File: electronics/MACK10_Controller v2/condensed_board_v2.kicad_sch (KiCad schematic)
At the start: 81 parts, among them J13 LOAD_CELL, J14 CHANNEL_B, J15 Motor, J16 AS5600 Encoder, J17 Fan, J18 Conn_01x02, J19 24V IN, J20 I/O, J21 LIM_TOP, J22 LIM_BOT, J23 INPUT, J24 E_STOP, J25 SSD1306, J26 Load Cell, J27 USER_STATUS_LED, J28 LOAD_CELL, Q3 MMBT3906, Q4 MMBT3906, U5 TMC2208, U8 HX711, U9 HX711

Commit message: Various PCB Schematic Updates
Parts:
- removed C10, C11, C12, C17, C18: 0.1uF, symbol Device:C
- removed C13, C15: 10uF, symbol Device:C
- removed J13: LOAD_CELL, symbol Connector_Generic:Conn_01x05
- removed J14: CHANNEL_B, symbol Connector_Generic:Conn_01x02
- removed J26: Load Cell, Connector_JST:JST_XH_B4B-XH-A_1x04_P2.50mm_Vertical, symbol MACK10:LOAD_CELL_4P
- removed JP3: Solder Jumper, symbol Jumper:SolderJumper_2_Bridged
- removed L2: 3.3uH, symbol Device:L
- removed Q3: MMBT3906, Package_TO_SOT_SMD:SOT-23, symbol Transistor_BJT:MMBT3906
- removed R10: 20k, symbol Device:R_US
- removed R11: 8.2k, symbol Device:R_US
- removed R12, R13: 100, symbol Device:R_US
- removed R14: 10k, symbol Device:R_US
- removed TP22: HX_SCK, TestPoint:TestPoint_Pad_2.0x2.0mm, symbol Connector:TestPoint
- removed TP23: HX_DT, TestPoint:TestPoint_Pad_2.0x2.0mm, symbol Connector:TestPoint
- removed U8: HX711, Package_SO:SOIC-16_3.9x9.9mm_P1.27mm, symbol Analog_ADC:HX711
- U9: symbol Analog_ADC:HX711 -> MACK10:HX711_IC
- renumbered J_EXPANSION to J_EXPANSION1
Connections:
- net 5V is gone; now on net +5V: J_EXPANSION1.3 (Pin_3)
- net +24V: now also U14.1 (VIN+); no longer U14. (VOUT-)
- net +5V: now also U14.3 (VOUT+); no longer U14. (VOUT-)
- net 3V3: now also U13.8 (VCC); no longer U13. (IN-)
- net GND: now also U13.7 (GND), U14.2 (VIN-), U14.4 (VOUT-); no longer C14.2, C16.2, U13. (IN-), U14. (VOUT-)
- net MOTOR_24V: now also U13.1 (IN+); no longer U13. (IN-)
- net MOTOR_VMOT: now also U13.2 (IN-), U13.3 (VBUS); no longer U13. (IN-)
- net SCL: now also U13.5 (SCL); no longer U13. (IN-)
- net SDA: now also U13.6 (SDA); no longer U13. (IN-)
- net UP: now also U12.8 (P00)
- net IO0: no longer names the net of J_EXPANSION1.6 (Pin_6)
- net IO0: no longer U12.8 (P00)
- new net: C14.2, C16.2
- no-connect marks 11 -> 22
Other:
- note removed: "AVDD = VBG(R1+R2)/R1"
- note removed: "Jumper Default: Closed Data rate set to 10SPS Open jumper to set to 80SPS Increases noise per read"
- moved on the sheet: C14, C16, C19, C21, C22, Q4, TP14, U5

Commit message: Minor PCB Changes
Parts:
- added J1, J2: Conn_02x05_Odd_Even, symbol Connector_Generic:Conn_02x05_Odd_Even
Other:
- moved on the sheet: J17, J24, J25, J27

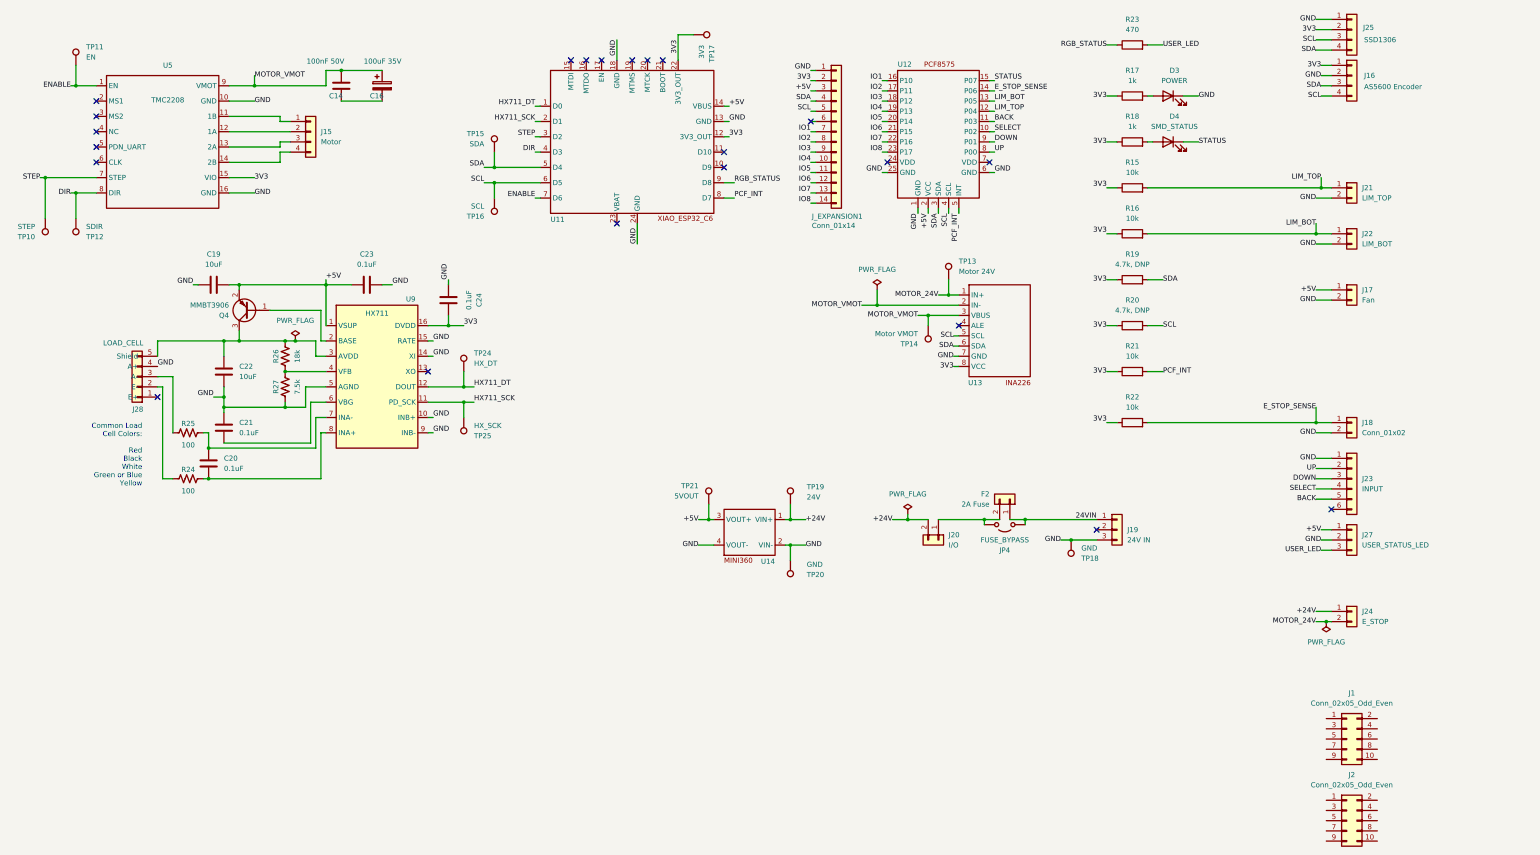
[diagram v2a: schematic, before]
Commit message: Updated Footprints and ERCs Passed
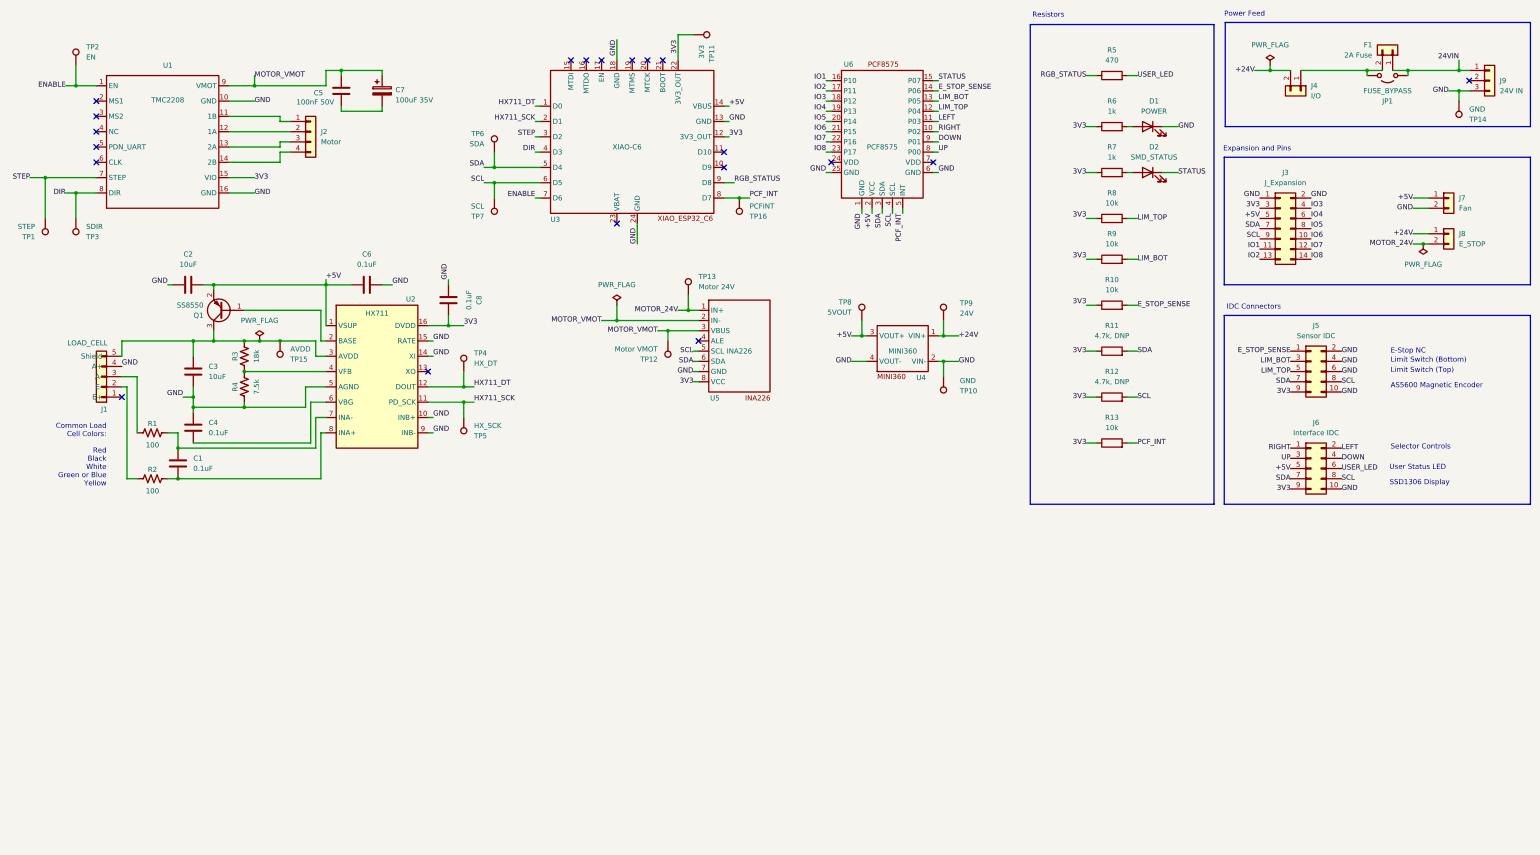
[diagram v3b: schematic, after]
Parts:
- removed J16: AS5600 Encoder, symbol Connector_Generic:Conn_01x04
- removed J18: Conn_01x02, symbol Connector_Generic:Conn_01x02
- removed J21: LIM_TOP, Connector_JST:JST_XH_B2B-XH-A_1x02_P2.50mm_Vertical, symbol Connector_Generic:Conn_01x02
- removed J22: LIM_BOT, Connector_JST:JST_XH_B2B-XH-A_1x02_P2.50mm_Vertical, symbol Connector_Generic:Conn_01x02
- removed J23: INPUT, Connector_JST:JST_XH_B6B-XH-A_1x06_P2.50mm_Vertical, symbol Connector_Generic:Conn_01x06
- removed J25: SSD1306, Connector_JST:JST_XH_B4B-XH-A_1x04_P2.50mm_Vertical, symbol Connector_Generic:Conn_01x04
- removed J27: USER_STATUS_LED, symbol Connector_Generic:Conn_01x03
- removed J_EXPANSION1: Conn_01x14, symbol Connector_Generic:Conn_01x14
- added J3: J_Expansion, Connector_PinHeader_2.54mm:PinHeader_2x07_P2.54mm_Vertical, symbol Connector_Generic:Conn_02x07_Odd_Even
- added TP15: AVDD, TestPoint:TestPoint_Pad_2.0x2.0mm, symbol Connector:TestPoint
- added TP16: PCFINT, TestPoint:TestPoint_Pad_2.0x2.0mm, symbol Connector:TestPoint
- C1: renamed from C20; footprint (none) -> Capacitor_SMD:C_0805_2012Metric
- C2: renamed from C19; footprint (none) -> Capacitor_SMD:C_0805_2012Metric
- C3: renamed from C22; footprint (none) -> Capacitor_SMD:C_0805_2012Metric
- C4: renamed from C21; footprint (none) -> Capacitor_SMD:C_0805_2012Metric
- C6: renamed from C23; footprint (none) -> Capacitor_SMD:C_0805_2012Metric
- C8: renamed from C24; footprint (none) -> Capacitor_SMD:C_0805_2012Metric
- J5: renamed from J2; value Conn_02x05_Odd_Even -> Sensor IDC; footprint (none) -> Connector_IDC:IDC-Header_2x05_P2.54mm_Vertical
- J6: renamed from J1; value Conn_02x05_Odd_Even -> Interface IDC; footprint (none) -> Connector_IDC:IDC-Header_2x05_P2.54mm_Vertical
- J7: renamed from J17; footprint (none) -> Connector_PinHeader_2.54mm:PinHeader_1x02_P2.54mm_Vertical
- Q1: renamed from Q4; value MMBT3906 -> SS8550; symbol Transistor_BJT:MMBT3906 -> Transistor_BJT:SS8550
- R1: renamed from R25; footprint (none) -> Resistor_SMD:R_0805_2012Metric
- R2: renamed from R24; footprint (none) -> Resistor_SMD:R_0805_2012Metric
- R3: renamed from R26; footprint (none) -> Resistor_SMD:R_0805_2012Metric
- R4: renamed from R27; footprint (none) -> Resistor_SMD:R_0805_2012Metric
- TP11: renamed from TP17; footprint (none) -> TestPoint:TestPoint_Pad_2.0x2.0mm
- TP12: renamed from TP14; footprint (none) -> TestPoint:TestPoint_Pad_2.0x2.0mm
- TP13: footprint (none) -> TestPoint:TestPoint_Pad_2.0x2.0mm
- TP14: renamed from TP18; footprint (none) -> TestPoint:TestPoint_Pad_2.0x2.0mm
- TP6: renamed from TP15; footprint (none) -> TestPoint:TestPoint_Pad_2.0x2.0mm
- TP7: renamed from TP16; footprint (none) -> TestPoint:TestPoint_Pad_2.0x2.0mm
- U3: renamed from U11; value (none) -> XIAO-C6; footprint (none) -> XIAO-SEEDSTUDIO:XIAO-ESP32-C6-SMD
- U4: renamed from U14; value (none) -> MINI360; footprint (none) -> Mini360:Mini360_step-down
- U5: renamed from U13; value (none) -> INA226; footprint (none) -> MACK10:INA226
- U6: renamed from U12; value (none) -> PCF8575; footprint (none) -> MACK10:PCF8575
- renumbered C14 to C5, C16 to C7, D3 to D1, D4 to D2, F2 to F1, J28 to J1, J15 to J2, J20 to J4, J24 to J8, J19 to J9, JP4 to JP1, R22 to R10, R19 to R11, R20 to R12, R21 to R13, R23 to R5, R17 to R6, R18 to R7, R15 to R8, R16 to R9, TP10 to TP1, TP20 to TP10, TP11 to TP2, TP12 to TP3, TP24 to TP4, TP25 to TP5, TP21 to TP8, TP19 to TP9, U5 to U1, U9 to U2
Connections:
- net BACK is gone; now on net LEFT: U6.11 (P03)
- net SELECT is gone; now on net RIGHT: U6.10 (P02)
- net +5V: now also J6.5 (Pin_5), J3.5 (Pin_5)
- net 3V3: now also J5.9 (Pin_9), J6.9 (Pin_9), J3.3 (Pin_3)
- net DOWN: now also J6.4 (Pin_4)
- net E_STOP_SENSE: now also J5.1 (Pin_1)
- net GND: now also J5.10 (Pin_10), J5.2 (Pin_2), J5.4 (Pin_4), J5.6 (Pin_6), J6.10 (Pin_10), J3.1 (Pin_1), J3.2 (Pin_2)
- net IO1: now also J3.11 (Pin_11)
- net IO2: now also J3.13 (Pin_13)
- net IO3: now also J3.4 (Pin_4)
- net IO4: now also J3.6 (Pin_6)
- net IO5: now also J3.8 (Pin_8)
- net IO6: now also J3.10 (Pin_10)
- net IO7: now also J3.12 (Pin_12)
- net IO8: now also J3.14 (Pin_14)
- net LIM_BOT: now also J5.3 (Pin_3)
- net LIM_TOP: now also J5.5 (Pin_5)
- net PCF_INT: now also TP16.1
- net SCL: now also J5.8 (Pin_8), J6.8 (Pin_8), J3.9 (Pin_9)
- net SDA: now also J5.7 (Pin_7), J6.7 (Pin_7), J3.7 (Pin_7)
- net UP: now also J6.3 (Pin_3)
- net USER_LED: now also J6.6 (Pin_6)
- net RIGHT: now reaches J6.1 (Pin_1)
- net LEFT: now reaches J6.2 (Pin_2)
- net at C3.1, J1.5 (Shield), Q1.3 (C)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: now also TP15.1
- no-connect marks 22 -> 20
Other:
- note added: "AS5600 Magnetic Encoder"
- note added: "E-Stop NC"
- note added: "Expansion and Pins"
- note added: "IDC Connectors"
- note added: "Limit Switch (Bottom)"
- note added: "Limit Switch (Top)"
- note added: "Power Feed"
- note added: "Resistors"
- note added: "SSD1306 Display"
- note added: "Selector Controls"
- note added: "User Status LED"
- moved on the sheet: C1, C2, C3, C4, C5, C7, D1, D2, F1, J1, J4, J5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

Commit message: First pass of PCB Layout (front and back)
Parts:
- removed TP10: GND, TestPoint:TestPoint_Pad_2.0x2.0mm, symbol Connector:TestPoint
- removed TP15: AVDD, TestPoint:TestPoint_Pad_2.0x2.0mm, symbol Connector:TestPoint
- removed TP16: PCFINT, TestPoint:TestPoint_Pad_2.0x2.0mm, symbol Connector:TestPoint
- removed TP2: EN, TestPoint:TestPoint_Pad_2.0x2.0mm, symbol Connector:TestPoint
- removed TP3: SDIR, TestPoint:TestPoint_Pad_2.0x2.0mm, symbol Connector:TestPoint
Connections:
- net +24V: now also U4.2 (VIN+); no longer U4.1 (VIN+)
- net +5V: now also U4.4 (VOUT+); no longer U4.3 (VOUT+)
- net GND: now also J9.2 (Pin_2), U4.1 (VIN-), U4.3 (VOUT-); no longer U4.2 (VIN-), U4.4 (VOUT-)
- no-connect marks 20 -> 19

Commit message: PCB Layout Finalization
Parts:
- added J10: BYP_2, Connector_PinHeader_2.54mm:PinHeader_1x02_P2.54mm_Vertical, symbol Connector_Generic:Conn_01x02
- D2: value SMD_STATUS -> STATUS
- F1: value 2A Fuse -> Fuse
- JP1: value FUSE_BYPASS -> BYP_1
- TP6: renamed from TP12; value Motor VMOT -> VMOT
- TP7: renamed from TP13; value Motor 24V -> M24V
- renumbered TP8 to TP10, TP14 to TP11, TP4 to TP2, TP5 to TP3, TP6 to TP4, TP7 to TP5, TP11 to TP8, U5 to U4, U6 to U5, U4 to U6
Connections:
- net MOTOR_24V: now also J10.1 (Pin_1)
- net MOTOR_VMOT: now also J10.2 (Pin_2)
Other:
- moved on the sheet: TP7

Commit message: Added EN for reboot, finishing touches
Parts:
- removed J1: LOAD_CELL, symbol Connector_Generic:Conn_01x05
- added SW1: ENABLE, Button_Switch_SMD:SW_SPST_CK_RS282G05A3, symbol Switch:SW_Push
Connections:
- net E_STOP_SENSE: now also J5.5 (Pin_5); no longer J5.1 (Pin_1)
- net GND: now also J5.1 (Pin_1), SW1.1; no longer J5.2 (Pin_2), J5.4 (Pin_4)
- net IO1: now also J3.4 (Pin_4); no longer J3.11 (Pin_11)
- net IO2: now also J3.6 (Pin_6); no longer J3.13 (Pin_13)
- net IO3: now also J3.8 (Pin_8); no longer J3.4 (Pin_4)
- net IO4: now also J3.10 (Pin_10); no longer J3.6 (Pin_6)
- net IO5: now also J3.12 (Pin_12); no longer J3.8 (Pin_8)
- net IO6: now also J3.14 (Pin_14); no longer J3.10 (Pin_10)
- net LIM_BOT: now also J3.13 (Pin_13); no longer J5.3 (Pin_3)
- net LIM_TOP: now also J3.11 (Pin_11); no longer J5.5 (Pin_5)
- net A+: now reaches R2.1
- net A+: now also J5.3 (Pin_3)
- net E+: now reaches C3.1, Q1.3 (C), R3.2, U2.3 (AVDD)
- net E+: now also J5.2 (Pin_2)
- net at U3.17 (EN): now also SW1.2
- net A-: now reaches R1.1
- net A-: now also J5.4 (Pin_4)
- net IO7: no longer names the net of U5.22 (P16)
- net IO7: no longer J3.12 (Pin_12)
- net IO8: no longer names the net of U5.23 (P17)
- net IO8: no longer J3.14 (Pin_14)
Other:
- note added: "Limit Switch (B)"
- note added: "Limit Switch (T)"
- note removed: "Limit Switch (Bottom)"
- note removed: "Limit Switch (Top)"
- moved on the sheet: J3, J7, J8

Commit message: All Checks Passed - V2 Sent for Manufacture
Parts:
- added D3: SS14, Diode_SMD:D_SMA, symbol Diode:1N5819
- SW1: value ENABLE -> RESET
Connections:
- net +5V: now also D3.2 (A); no longer U3.14 (VBUS)
- new net: D3.1 (K), U3.14 (VBUS)
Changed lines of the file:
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@@
 	)
 	(junction
+		(at 208.28 39.37)
+		(diameter 0)
+		(color 0 0 0 0)
+	)
+	(junction
 		(at 384.81 38.1)
 		(diameter 0)
@@
 	(wire
 		(pts
+			(xy 208.28 24.13) (xy 208.28 26.67)
+		)
+		(stroke
+			(width 0)
+			(type default)
+		)
+	)
+	(wire
+		(pts
 			(xy 255.27 105.41) (xy 256.54 105.41)
 		)
@@
 	(wire
 		(pts
+			(xy 208.28 34.29) (xy 208.28 39.37)
+		)
+		(stroke
+			(width 0)
+			(type default)
+		)
+	)
+	(wire
+		(pts
 			(xy 128.27 111.76) (xy 137.16 111.76)
 		)
@@
 	(wire
 		(pts
+			(xy 201.93 41.91) (xy 208.28 41.91)
+		)
+		(stroke
+			(width 0)
+			(type default)
+		)
+	)
+	(wire
+		(pts
 			(xy 254 50.8) (xy 255.27 50.8)
 		)
@@
 	(wire
 		(pts
-			(xy 201.93 41.91) (xy 203.2 41.91)
-		)
-		(stroke
-			(width 0)
-			(type default)
-		)
-	)
-	(wire
-		(pts
 			(xy 384.81 33.02) (xy 387.35 33.02)
 		)
@@
 	(wire
 		(pts
+			(xy 208.28 39.37) (xy 208.28 41.91)
+		)
+		(stroke
+			(width 0)
+			(type default)
+		)
+	)
+	(wire
+		(pts
 			(xy 99.06 115.57) (xy 102.87 115.57)
 		)
@@
 		)
 	)
-	(label "+5V"
-		(at 203.2 41.91 0)
-		(effects
-			(font
-				(size 1.27 1.27)
-			)
-			(justify left bottom)
-		)
-	)
 	(label "MOTOR_24V"
 		(at 187.96 85.09 180)
@@
 	)
 	(label "+5V"
+		(at 208.28 24.13 0)
+		(effects
+			(font
+				(size 1.27 1.27)
+			)
+			(justify left bottom)
+		)
+	)
+	(label "+5V"
 		(at 382.27 64.77 180)
 		(fields_autoplaced yes)
@@
 	)
 	(symbol
+		(lib_id "Diode:1N5819")
+		(at 208.28 30.48 90)
+		(unit 1)
+		(body_style 1)
+		(exclude_from_sim no)
+		(in_bom yes)
+		(on_board yes)
+		(in_pos_files yes)
+		(dnp no)
+		(fields_autoplaced yes)
+		(property "Reference" "D3"
+			(at 210.82 29.5274 90)
+			(show_name no)
+			(do_not_autoplace no)
+			(effects
+				(font
+					(size 1.27 1.27)
+				)
+				(justify right)
+			)
+		)
+		(property "Value" "SS14"
+			(at 210.82 32.0674 90)
+			(show_name no)
+			(do_not_autoplace no)
+			(effects
+				(font
+					(size 1.27 1.27)
+				)
+				(justify right)
+			)
+		)
+		(property "Footprint" "Diode_SMD:D_SMA"
+			(at 212.725 30.48 0)
+			(hide yes)
+			(show_name no)
+			(do_not_autoplace no)
+			(effects
+				(font
+					(size 1.27 1.27)
+				)
+			)
+		)
+		(property "Datasheet" "http://www.vishay.com/docs/88525/1n5817.pdf"
+			(at 208.28 30.48 0)
+			(hide yes)
+			(show_name no)
+			(do_not_autoplace no)
+			(effects
+				(font
+					(size 1.27 1.27)
+				)
+			)
+		)
+		(property "Description" "40V 1A Schottky Barrier Rectifier Diode, DO-41"
+			(at 208.28 30.48 0)
+			(hide yes)
+			(show_name no)
+			(do_not_autoplace no)
+			(effects
+				(font
+					(size 1.27 1.27)
+				)
+			)
+		)
+		(pin "1"
+		)
+		(pin "2"
+		)
+		(instances
+			(project "MACK10_Controller"
+				(path "/b4040018-4e12-4890-8820-9e52ff91a3d0"
+					(reference "D3")
+					(unit 1)
+				)
+			)
+		)
+	)
+	(symbol
 		(lib_id "Device:R")
 		(at 298.45 34.29 90)
@@
 	)
 	(symbol
+		(lib_id "power:PWR_FLAG")
+		(at 208.28 39.37 270)
+		(unit 1)
+		(body_style 1)
+		(exclude_from_sim no)
+		(in_bom yes)
+		(on_board yes)
+		(in_pos_files yes)
+		(dnp no)
+		(property "Reference" "#FLG05"
+			(at 210.185 39.37 0)
+			(hide yes)
+			(show_name no)
+			(do_not_autoplace no)
+			(effects
+				(font
+					(size 1.27 1.27)
+				)
+			)
+		)
+		(property "Value" "PWR_FLAG"
+			(at 213.36 39.37 0)
+			(show_name no)
+			(do_not_autoplace no)
+			(effects
+				(font
+					(size 1.27 1.27)
+				)
+			)
+		)
+		(property "Footprint" ""
+			(at 208.28 39.37 0)
+			(hide yes)
+			(show_name no)
+			(do_not_autoplace no)
+			(effects
+				(font
+					(size 1.27 1.27)
+				)
+			)
+		)
+		(property "Datasheet" ""
+			(at 208.28 39.37 0)
+			(hide yes)
+			(show_name no)
+			(do_not_autoplace no)
+			(effects
+				(font
+					(size 1.27 1.27)
+				)
+			)
+		)
+		(property "Description" "Special symbol for telling ERC where power comes from"
+			(at 208.28 39.37 0)
+			(hide yes)
+			(show_name no)
+			(do_not_autoplace no)
+			(effects
+				(font
+					(size 1.27 1.27)
+				)
+			)
+		)
+		(pin "1"
+		)
+		(instances
+			(project "MACK10_Controller"
+				(path "/b4040018-4e12-4890-8820-9e52ff91a3d0"
+					(reference "#FLG05")
+					(unit 1)
+				)
+			)
+		)
+	)
+	(symbol
 		(lib_id "Connector:TestPoint")
 		(at 384.81 40.64 0)
@@
 			)
 		)
-		(property "Value" "ENABLE"
+		(property "Value" "RESET"
 			(at 165.1 20.32 0)
 			(show_name no)
